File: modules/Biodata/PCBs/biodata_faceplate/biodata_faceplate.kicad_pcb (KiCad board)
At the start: 2 copper layers, 60.6 x 128.5 mm, 1 part

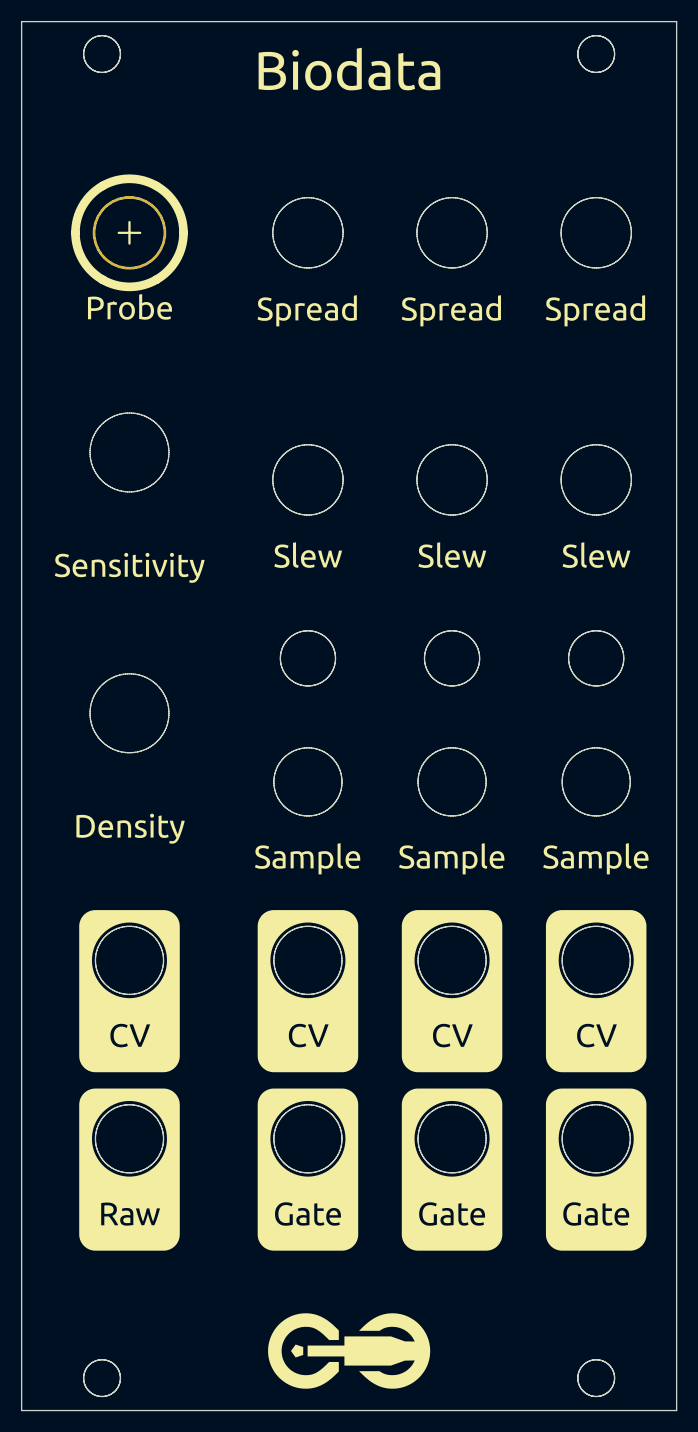
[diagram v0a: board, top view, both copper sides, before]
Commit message: Update biodata facepalte PCB to 6HP version
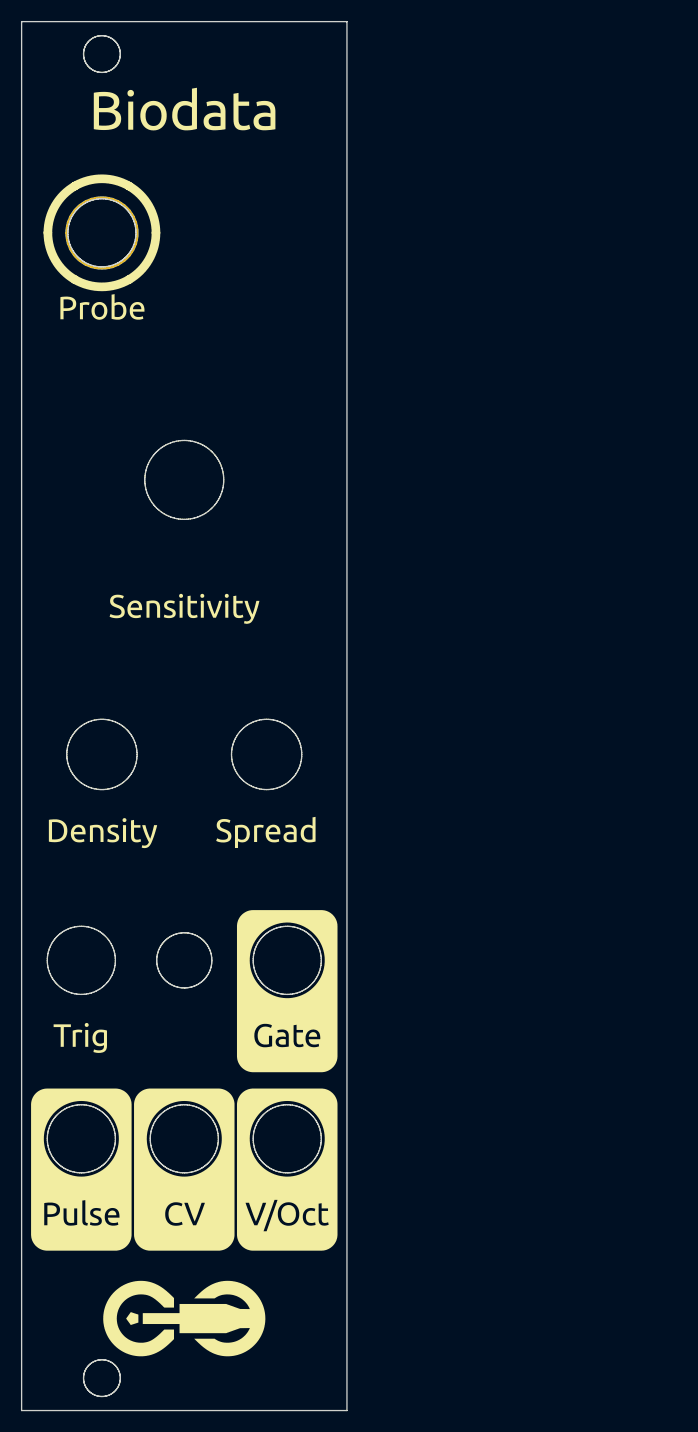
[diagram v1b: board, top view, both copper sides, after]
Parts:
- moved REF** 2.55 mm to (70.9, 51.3)
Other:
- board size 60.6 x 128.5 mm -> 30.1 x 128.5 mm
